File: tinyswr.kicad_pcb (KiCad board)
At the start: 2 copper layers, 20.8 x 14.2 mm, 15 parts, among them J1 ANT, J2 RIG

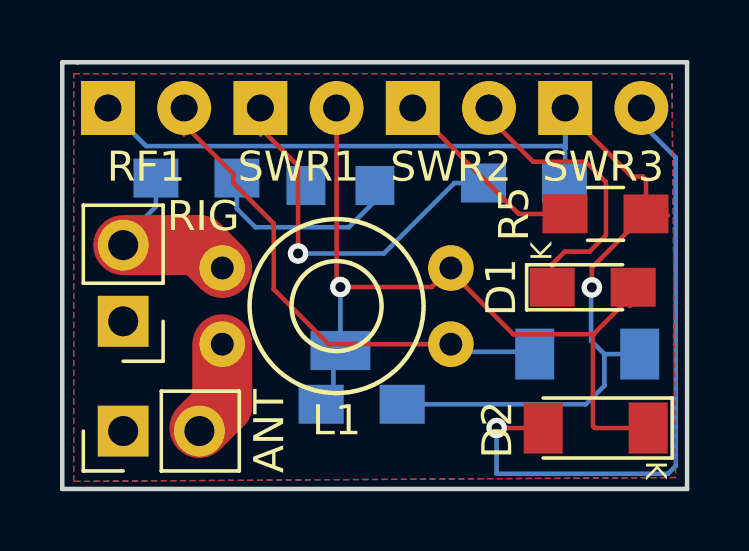
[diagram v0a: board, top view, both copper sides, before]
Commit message: fixed missing gnd connection and other bugs
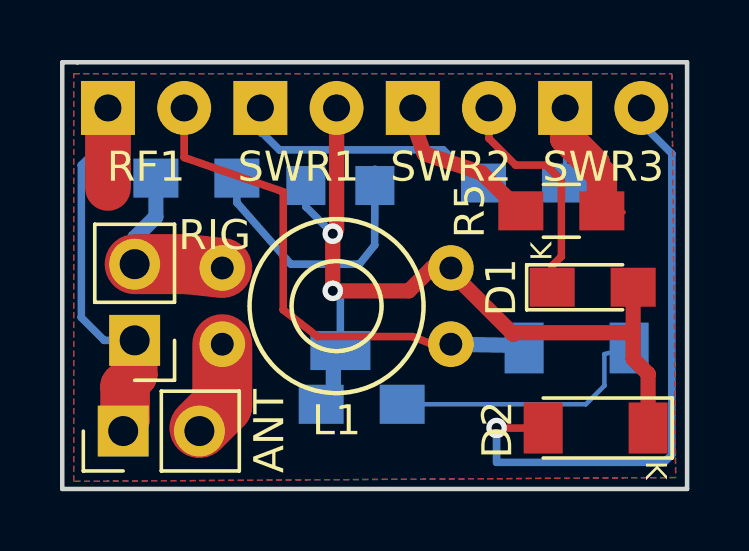
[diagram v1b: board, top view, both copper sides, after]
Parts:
- R4: value 860 -> 820
- moved R5 1.48 mm to (168.7, 98.6)
- moved J2 0.74 mm to (154.4, 102.9)
- moved D3 0.41 mm to (169.2, 103.1)
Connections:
- D3 pad 2: Net-(D3-Pad2) -> GND
- R2 pad 3: (no net) -> Net-(D1-Pad2)
- R3 pad 2: Net-(D3-Pad2) -> GND
- R4 pad 2: Net-(D3-Pad2) -> GND
- R5 pad 2: Net-(D3-Pad2) -> GND
- RF1 pad 1: Net-(D3-Pad2) -> GND
- SWR3 pad 1: Net-(D3-Pad2) -> GND
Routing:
- net GND: track 0.00 -> 43.9 mm
- net Net-(D3-Pad2): track 40.8 -> 0.00 mm, vias 1 -> 0
- net Net-(D1-Pad2): track 28.8 -> 33.3 mm, vias 1 -> 2
- net Net-(R1-Pad2): track 6.76 -> 9.70 mm
- net Net-(R4-Pad1): track 13.4 -> 10.5 mm, vias 1 -> 0
- net Net-(D3-Pad1): track 18.0 -> 19.9 mm
- net Net-(D1-Pad1): track 11.0 -> 9.93 mm
- net Net-(D2-Pad2): track 22.0 -> 21.0 mm
- net Net-(R5-Pad1): track 6.54 -> 5.63 mm
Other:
- net class 10mil added: clearance 0.1524, trace_width 0.254, via_dia 0.6858, via_drill 0.3302
- board text added: "Rev 1.2 2017-10-24"
- board text removed: "Rev 1.1 2017-09-13"
